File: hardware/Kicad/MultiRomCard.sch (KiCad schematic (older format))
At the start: 9 parts, among them P1 VC4000_Cartridge_Bus, U1 Arduino_UNO, U2 74HC595, U3 74HC595, U4 74HC595, U5 6264, U6 74HC245, U7 74HC245, U8 74HC245

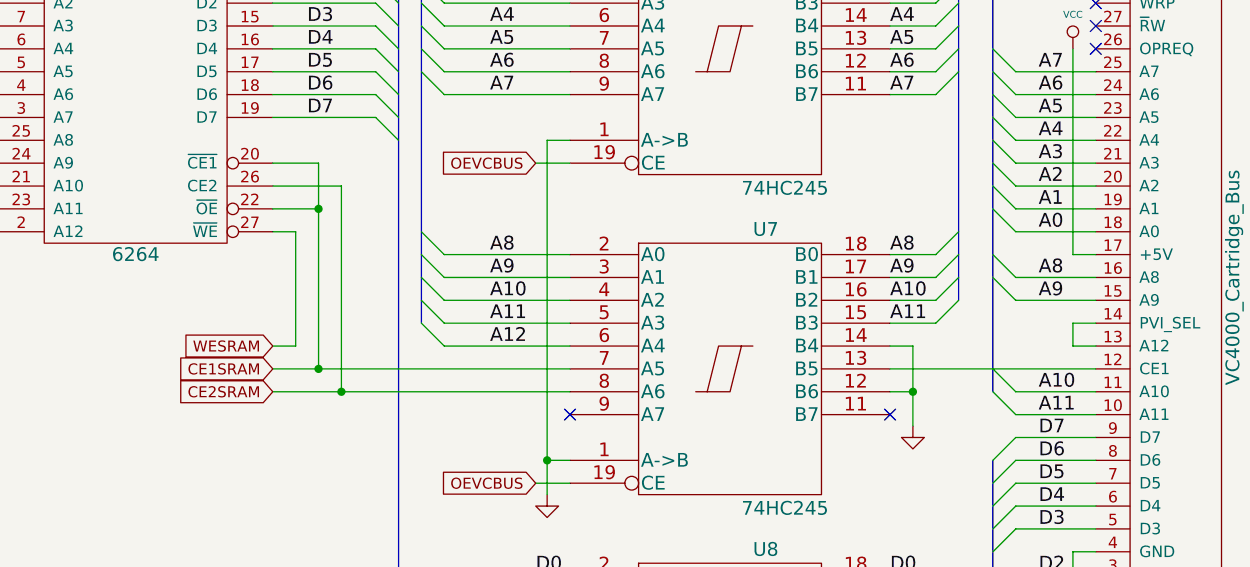
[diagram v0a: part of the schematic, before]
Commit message: updated SRAM /CE1 & CE2 connection to Arduino and bus transceiver
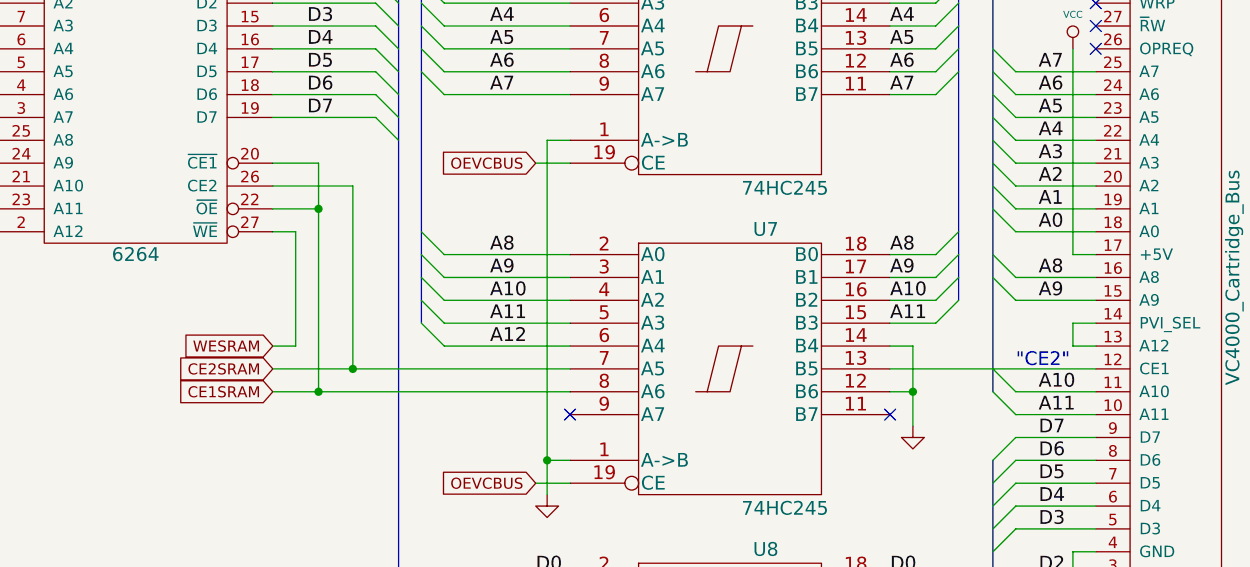
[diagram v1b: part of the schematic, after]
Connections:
- net CE1SRAM: now also U7.8 (A6); no longer U7.7 (A5)
- net CE2SRAM: now also U7.7 (A5); no longer U7.8 (A6)
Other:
- note added: ""CE2""
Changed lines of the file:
@@
 	6750 3050 6950 3050
 Wire Wire Line
-	6950 2850 6950 3750
-Wire Wire Line
-	6750 2950 7050 2950
-Wire Wire Line
-	7050 2950 7050 3850
+	6950 2850 6950 3850
 Wire Bus Line
 	7300 2050 7300 5550
@@
 	2200 3500 2300 3500
 Text GLabel 6750 3750 0    48   Input ~ 0
+CE2SRAM
+Text GLabel 6750 3850 0    48   Input ~ 0
 CE1SRAM
-Text GLabel 6750 3850 0    48   Input ~ 0
-CE2SRAM
 NoConn ~ 2200 4300
 NoConn ~ 2200 4200
@@
 Wire Wire Line
 	6750 3850 8050 3850
-Connection ~ 7050 3850
 $Comp
 L GND #PWR07
@@
 Wire Wire Line
 	9550 3850 9450 3850
-Connection ~ 6950 3750
 Wire Wire Line
 	9450 3750 10350 3750
@@
 	1    0    0    -1
 $EndComp
+Connection ~ 6950 3850
+Wire Wire Line
+	6750 2950 7100 2950
+Wire Wire Line
+	7100 2950 7100 3750
+Connection ~ 7100 3750
+Text Notes 10000 3750 0    60   ~ 0
+"CE2"
 $EndSCHEMATC

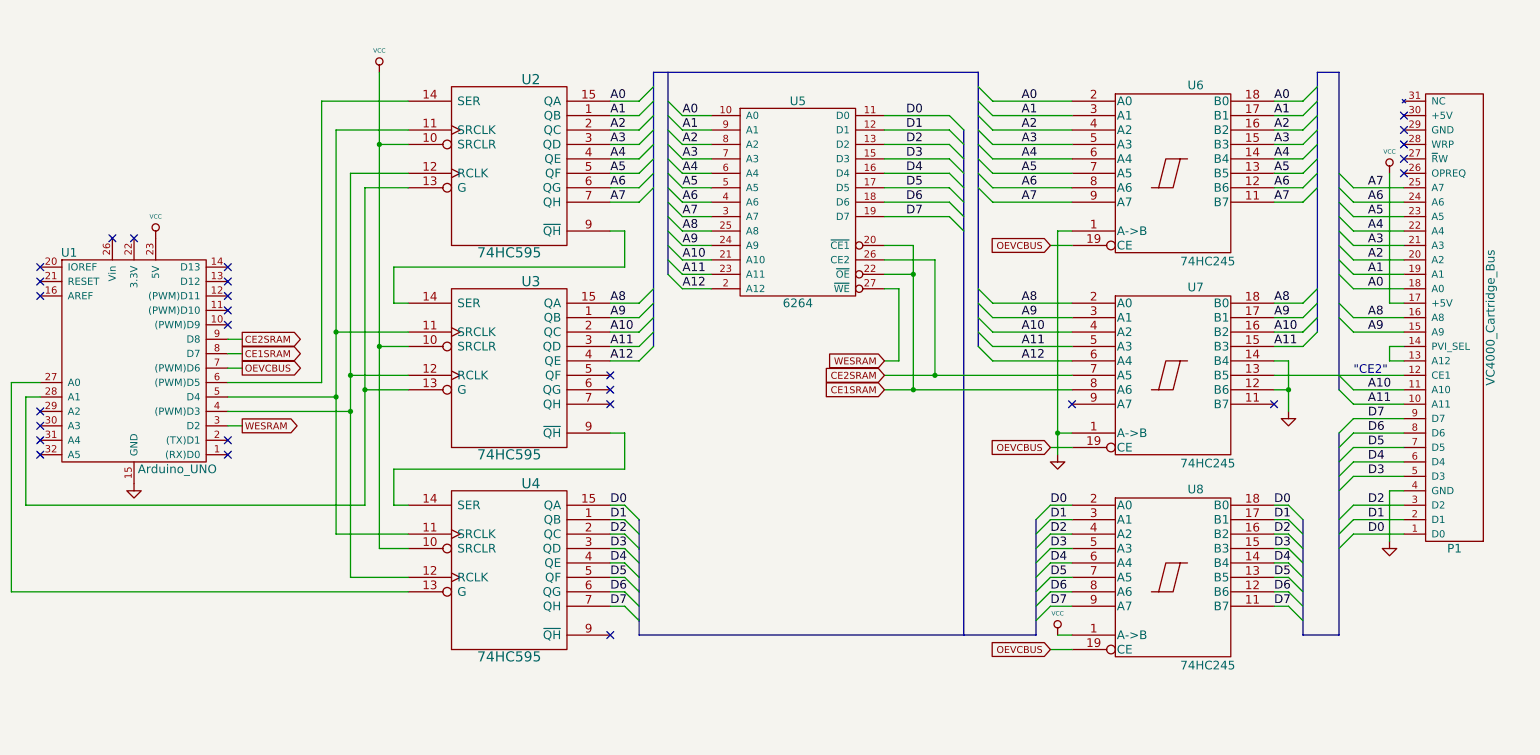
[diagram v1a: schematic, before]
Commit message: Updated date string in Schematic.
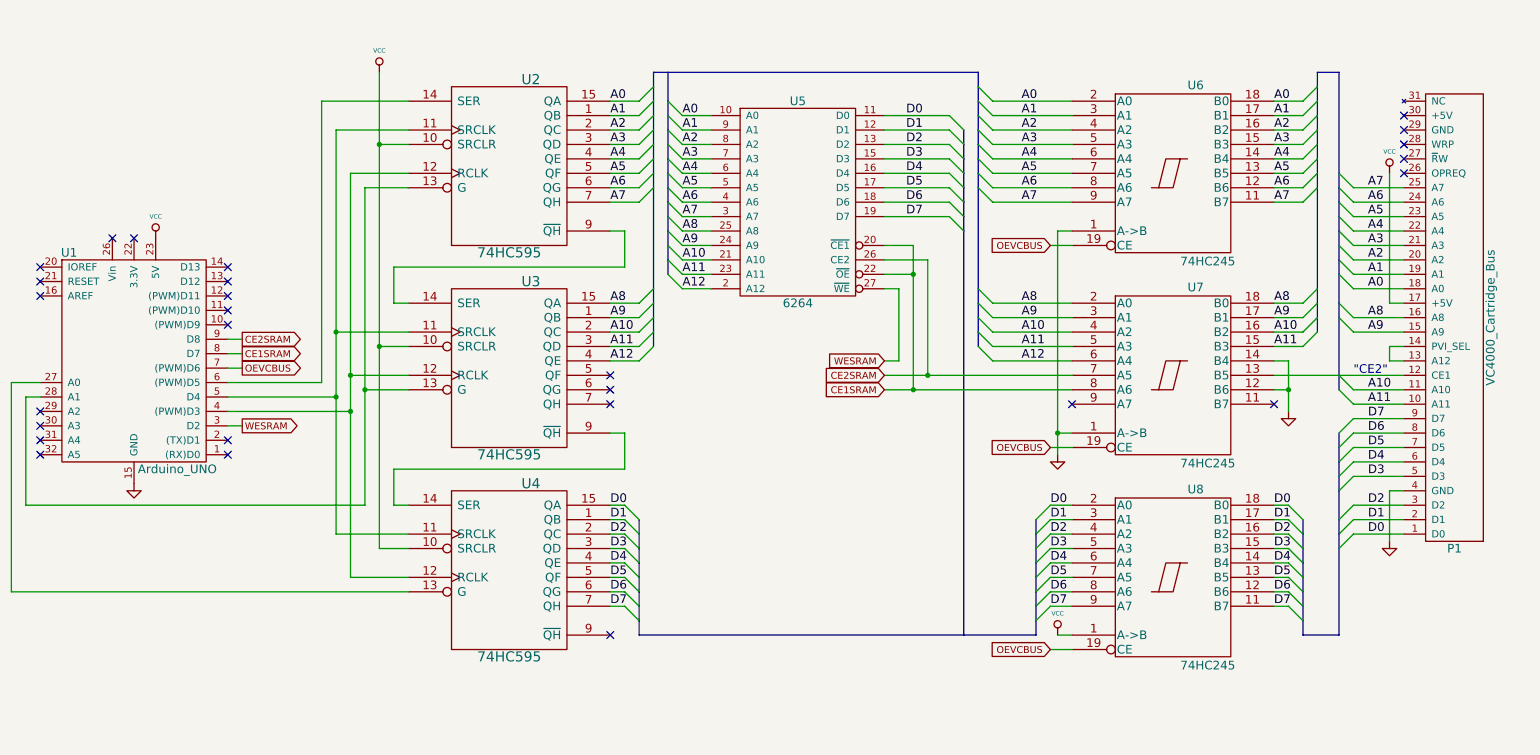
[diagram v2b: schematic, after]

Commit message: Preparations for PCB layout
- Created footprints for Cartridge Bus and Arduino UNO,
- Modified Arduino UNO schematic symbol to include pin numbers,
- Created initial netlist, and
- Spread all footprints on board, no traces yet.
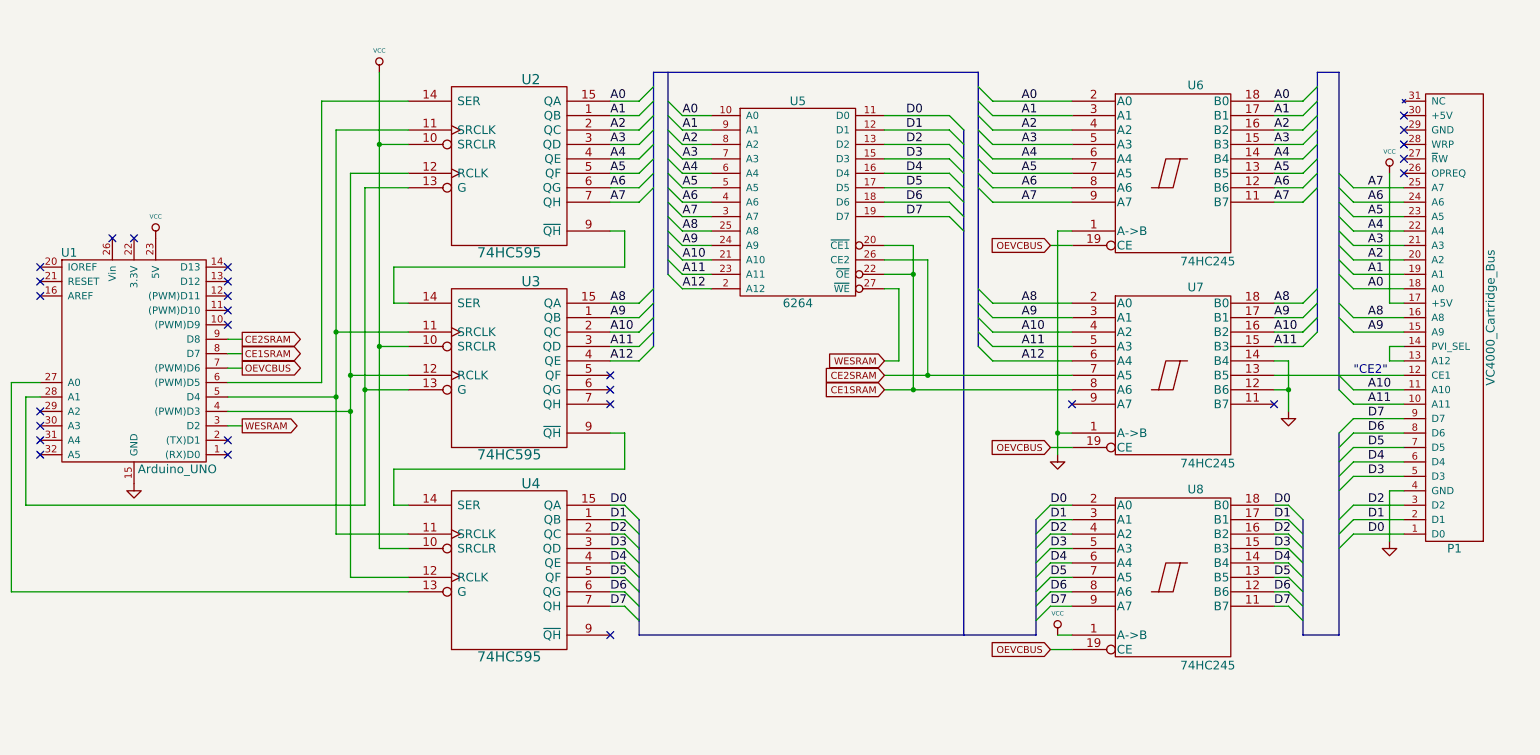
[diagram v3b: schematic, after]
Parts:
- P1: footprint (none) -> VC4000_MultiRom:VC4000_CartridgeBus
- U1: footprint (none) -> VC4000_MultiRom:Arduino_UNO
- U2, U3, U4: footprint (none) -> Housings_DIP:DIP-16__300_ELL
- U5: footprint (none) -> Housings_DIP:DIP-28__600_ELL
- U6, U7, U8: footprint (none) -> Housings_DIP:DIP-20__300_ELL

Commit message: Euro PCB outline and some part changes (BREAKS CURRENT FIRMWARE!)
- Swapped A and B sides on Bus transcievers for easier tracing.
  (Not sure if this is ideal, yet, but certainly better than
  before!). THIS BREAKS CURRENT FIRMWARE! Need to change
  direction bits!
- Prefix bus labels from the cartridge to the transcievers with 'E'
  (for 'external') to de-confuse Pcbnew.
- Connect second +5V and GND connectors to power nets for easier
  board connections.
- revert previous changes to cartridge bus footprint.
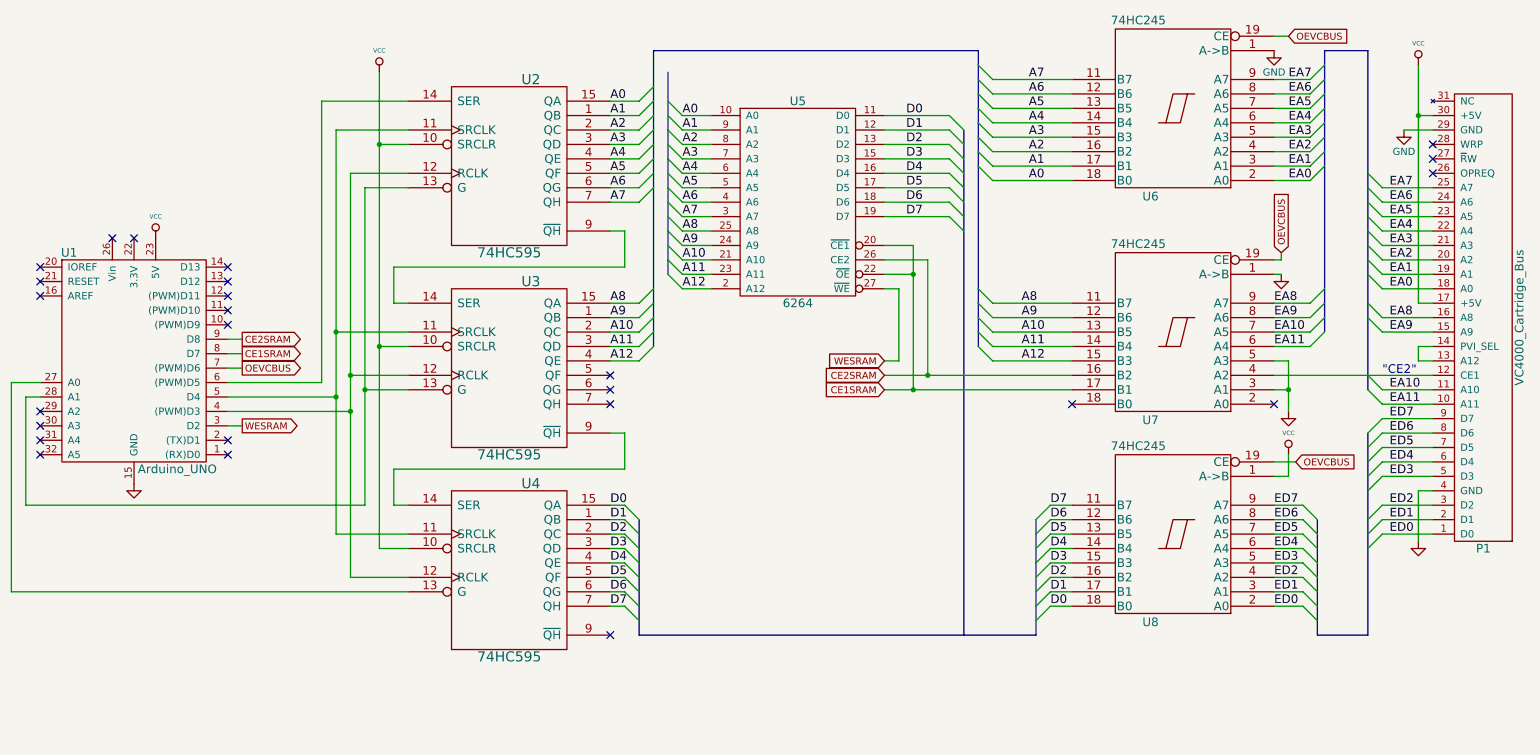
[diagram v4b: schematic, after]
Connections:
- net A0: no longer P1.18 (A0), U6.2 (A0)
- net A1: no longer P1.19 (A1), U6.3 (A1)
- net A10: now also U7.13 (B5); no longer P1.11 (A10), U7.16 (B2), U7.4 (A2)
- net A11: now also U7.14 (B4); no longer P1.10 (A11), U7.15 (B3), U7.5 (A3)
- net A12: now also U7.15 (B3); no longer U7.6 (A4)
- net A2: no longer P1.20 (A2), U6.4 (A2)
- net A3: no longer P1.21 (A3), U6.5 (A3)
- net A4: no longer P1.22 (A4), U6.6 (A4)
- net A5: no longer P1.23 (A5), U6.7 (A5)
- net A6: no longer P1.24 (A6), U6.8 (A6)
- net A7: no longer P1.25 (A7), U6.9 (A7)
- net A8: now also U7.11 (B7); no longer P1.16 (A8), U7.18 (B0), U7.2 (A0)
- net A9: now also U7.12 (B6); no longer P1.15 (A9), U7.17 (B1), U7.3 (A1)
- net CE1SRAM: now also U7.17 (B1); no longer U7.8 (A6)
- net CE2SRAM: now also U7.16 (B2); no longer U7.7 (A5)
- net D0: no longer P1.1 (D0), U8.2 (A0)
- net D1: no longer P1.2 (D1), U8.3 (A1)
- net D2: no longer P1.3 (D2), U8.4 (A2)
- net D3: no longer P1.5 (D3), U8.5 (A3)
- net D4: no longer P1.6 (D4), U8.6 (A4)
- net D5: no longer P1.7 (D5), U8.7 (A5)
- net D6: no longer P1.8 (D6), U8.8 (A6)
- net D7: no longer P1.9 (D7), U8.9 (A7)
- net GND: now also P1.29 (GND), U7.3 (A1), U7.5 (A3); no longer U7.12 (B6), U7.14 (B4)
- net VCC: now also P1.30 (+5V)
- net at P1.12 (CE1): now also U7.4 (A2); no longer U7.13 (B5)
- net EA8: now reaches U7.9 (A7)
- net EA8: now also P1.16 (A8)
- new net EA0: P1.18 (A0), U6.2 (A0)
- new net EA1: P1.19 (A1), U6.3 (A1)
- new net EA10: P1.11 (A10), U7.7 (A5)
- new net EA11: P1.10 (A11), U7.6 (A4)
- new net EA2: P1.20 (A2), U6.4 (A2)
- new net EA3: P1.21 (A3), U6.5 (A3)
- new net EA4: P1.22 (A4), U6.6 (A4)
- new net EA5: P1.23 (A5), U6.7 (A5)
- new net EA6: P1.24 (A6), U6.8 (A6)
- new net EA7: P1.25 (A7), U6.9 (A7)
- new net EA9: P1.15 (A9), U7.8 (A6)
- new net ED0: P1.1 (D0), U8.2 (A0)
- new net ED1: P1.2 (D1), U8.3 (A1)
- new net ED2: P1.3 (D2), U8.4 (A2)
- new net ED3: P1.5 (D3), U8.5 (A3)
- new net ED4: P1.6 (D4), U8.6 (A4)
- new net ED5: P1.7 (D5), U8.7 (A5)
- new net ED6: P1.8 (D6), U8.8 (A6)
- new net ED7: P1.9 (D7), U8.9 (A7)
- no-connect marks 27 -> 25
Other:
- moved on the sheet: P1, U6, U7, U8
